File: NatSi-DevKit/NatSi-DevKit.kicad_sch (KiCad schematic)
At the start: 0 parts

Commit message: git ignore not working?
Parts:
- added U?: ESP32-S3-WROOM-1, PCM_Espressif:ESP32-S3-WROOM-1, symbol sumec_sch_lib:ESP32-S3-WROOM-1_CUSTOM_made_by_bismarx
- added U?: NCP1117-3.3_SOT223, Package_TO_SOT_SMD:SOT-223-3_TabPin2, symbol Regulator_Linear:NCP1117-3.3_SOT223
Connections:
- new net: U?.1 (GND), U?.40 (GND), U?.41 (GND)
- new net +3V3: U?.2 (3V3)

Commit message: some updates schematic
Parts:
- added C? (x3): 10uF, Capacitor_Tantalum_SMD:CP_EIA-3216-18_Kemet-A_Pad1.58x1.35mm_HandSolder, symbol Device:C_Polarized
- added C?: 100nF, Capacitor_SMD:C_0805_2012Metric_Pad1.18x1.45mm_HandSolder, symbol Device:C
- added J?: TYPE-C-31-M-12 (USB C CONN), TYPE-C-31-M-12:HRO_TYPE-C-31-M-12, symbol SchrackThingy_library:TYPE-C-31-M-12 (USB C CONN)
- gave numbers to parts that had none: 2
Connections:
- net +3V3: now also C?.1, C?.1
- net GND: now also U1.1 (GND), U1.40 (GND), U1.41 (GND), U2.1 (GND), C?.2, C?.2, C?.2, C?.2, J?.A1_B12 (GND), J?.B1_A12 (GND), J?.S1 (SHIELD), J?.S2 (SHIELD), J?.S3 (SHIELD), J?.S4 (SHIELD)
- net IO17: now reaches U1.10 (IO17)
- net IO18: now reaches U1.11 (IO18)
- net D-: now reaches U1.13 (IO19)
- net D+: now reaches U1.14 (IO20)
- net IO03: now reaches U1.15 (IO3)
- net IO42: now reaches U1.16 (IO46)
- net IO42: now also U1.35 (IO42)
- net IO21: now reaches U1.23 (IO21)
- net IO47: now reaches U1.24 (IO47)
- net IO48: now reaches U1.25 (IO48)
- net IO45: now reaches U1.26 (IO45)
- net BOOT: now reaches U1.27 (IO0)
- net IO35: now reaches U1.28 (IO35)
- net IO36: now reaches U1.29 (IO36)
- net EN: now reaches U1.3 (EN)
- net IO37: now reaches U1.30 (IO37)
- net IO38: now reaches U1.31 (IO38)
- net IO39: now reaches U1.32 (IO39)
- net IO40: now reaches U1.33 (IO40)
- net IO41: now reaches U1.34 (IO41)
- net RX: now reaches U1.36 (RXD0)
- net TX: now reaches U1.37 (TXD0)
- net IO02: now reaches U1.38 (IO2)
- net IO01: now reaches U1.39 (IO1)
- net +3.3V: now reaches U2.2 (VO)
- net +3.3V: now also C?.1
- net +5V: now reaches U2.3 (VI)
- net +5V: now also C?.1
- new net: J?.A4_B9 (VBUS), J?.B4_A9 (VBUS)
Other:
- moved on the sheet: U2

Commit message: update git ignore
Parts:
- removed J?: TYPE-C-31-M-12 (USB C CONN), TYPE-C-31-M-12:HRO_TYPE-C-31-M-12, symbol SchrackThingy_library:TYPE-C-31-M-12 (USB C CONN)
- added C?: 100nF, Capacitor_SMD:C_0805_2012Metric_Pad1.18x1.45mm_HandSolder, symbol Device:C
- added F?: Polyfuse/50R, Fuse:Fuse_0805_2012Metric, symbol Device:Polyfuse
- added J?: USB_TypeC, sumec_brd:USB_Type_C, symbol sumec_sch_lib:USB_TypeC
- added R? (x2): 15R, Resistor_SMD:R_0805_2012Metric_Pad1.20x1.40mm_HandSolder, symbol Device:R
- added U?: USBLC6-2SC6, Package_TO_SOT_SMD:TSOT-23-6_HandSoldering, symbol sumec_library:USBLC6-2SC6
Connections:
- net D+: now also U?.6
- net D-: now also U?.4
- net GND: now also C?.2, J?.A1_B12 (GND), J?.B1_A12 (GND), J?.S1 (SHIELD), J?.S2 (SHIELD), J?.S3 (SHIELD), J?.S4 (SHIELD), U?.2
- net IO04: now also U1.4 (IO4)
- net IO05: now also U1.5 (IO5)
- net IO06: now also U1.6 (IO6)
- net IO07: now also U1.7 (IO7)
- net IO08: now also U1.12 (IO8)
- net IO09: now also U1.17 (IO9)
- net IO10: now also U1.18 (IO10)
- net IO11: now also U1.19 (IO11)
- net IO12: now also U1.20 (IO12)
- net IO13: now also U1.21 (IO13)
- net IO14: now also U1.22 (IO14)
- net IO15: now also U1.8 (IO15)
- net IO16: now also U1.9 (IO16)
- new net: F?.2, J?.A4_B9 (VBUS), J?.B4_A9 (VBUS)
- new net: R?.2, U?.3
- new net: R?.2, U?.1
- new net D+ IN: J?.A6 (DP1), J?.B6 (DP2), R?.1
- new net D- IN: J?.A7 (DN1), J?.B7 (DN2), R?.1
- new net VBUS 5V: C?.1, F?.1, U?.5
- no-connect marks 0 -> 4
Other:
- note added: "ESD PROTECTION"
- note added: "GPIO USB 20 D+ (green) 19 D- (white) GND GND (black) VBUS +5V (red)"
- note added: "USB"
- note added: "USB CONNECTOR"
- note added: "USB Type-C Connector Data transfer USB connector connected to ESP32 using CDC method"

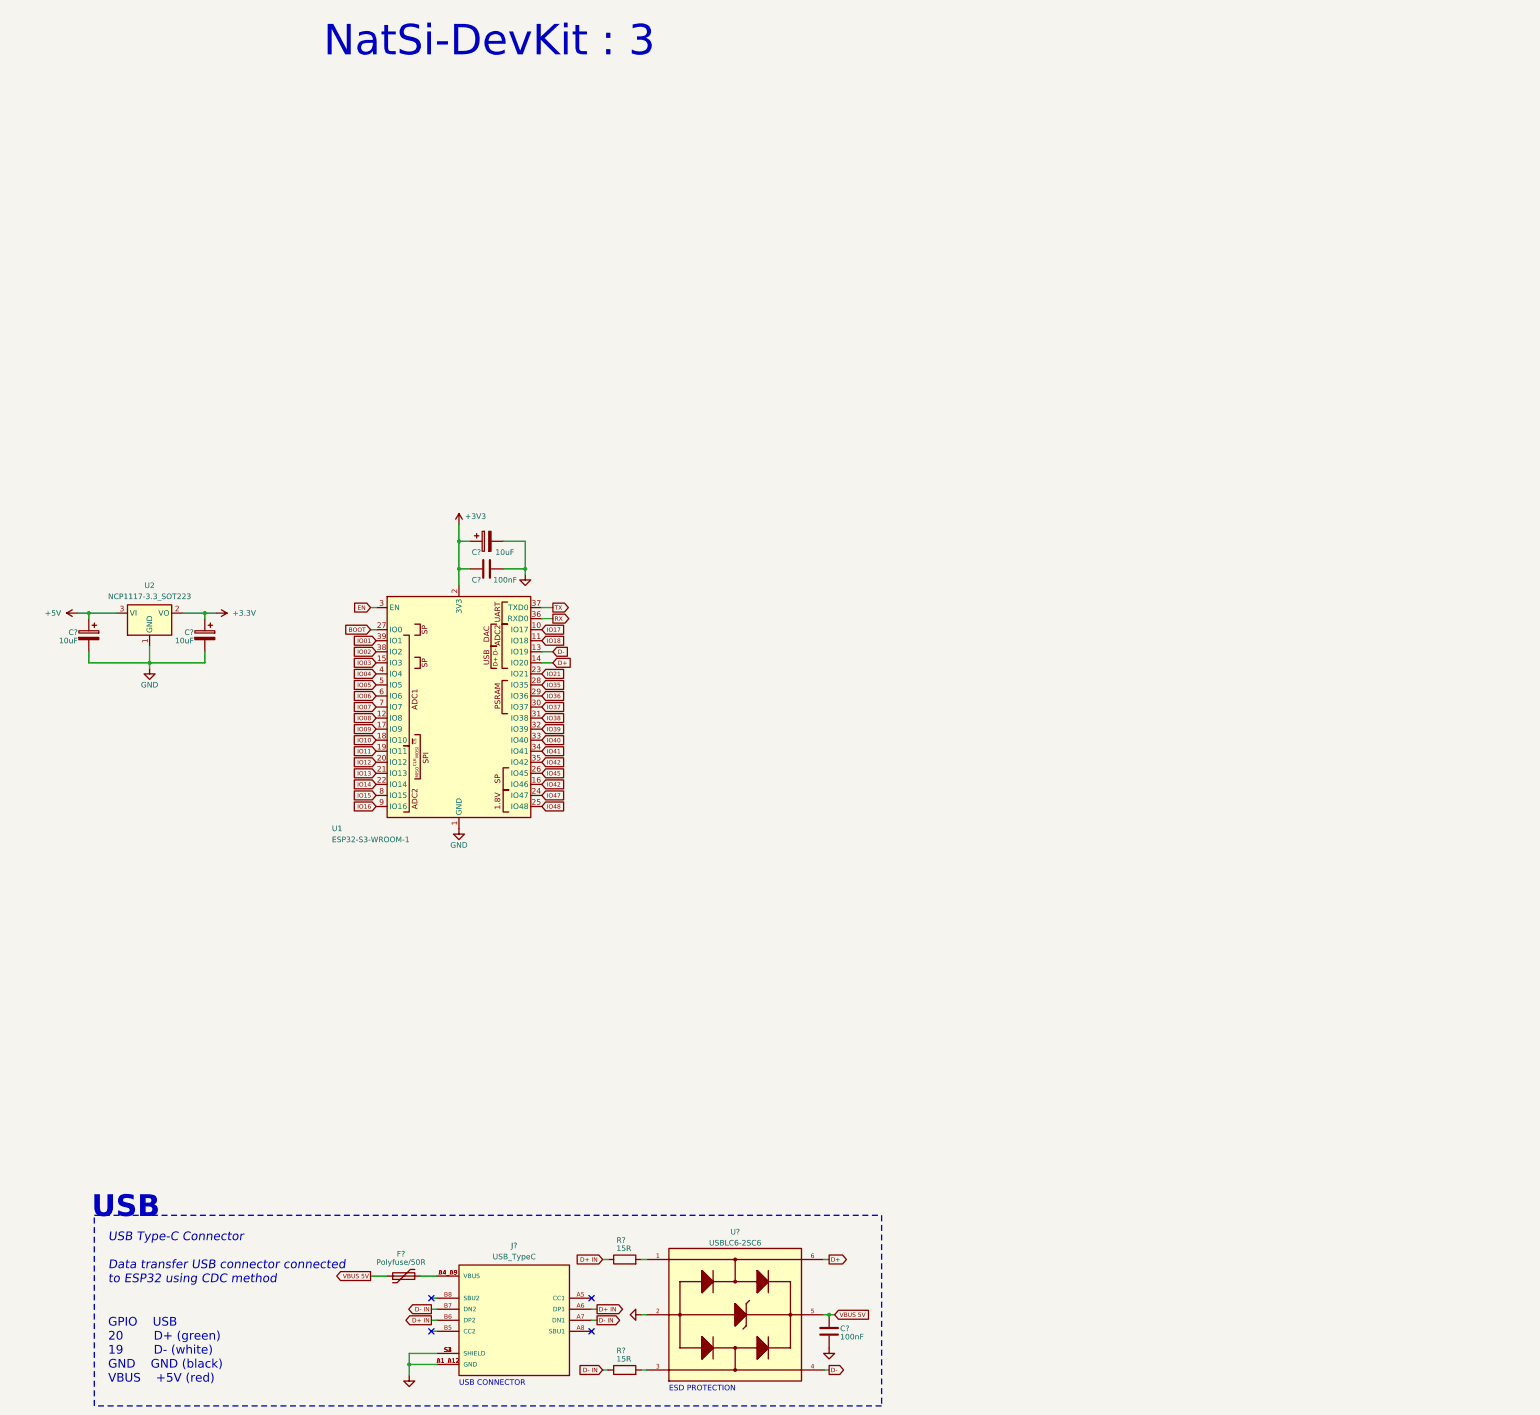
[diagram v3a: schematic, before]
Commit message: Schematic update
Blocks, schematic finished
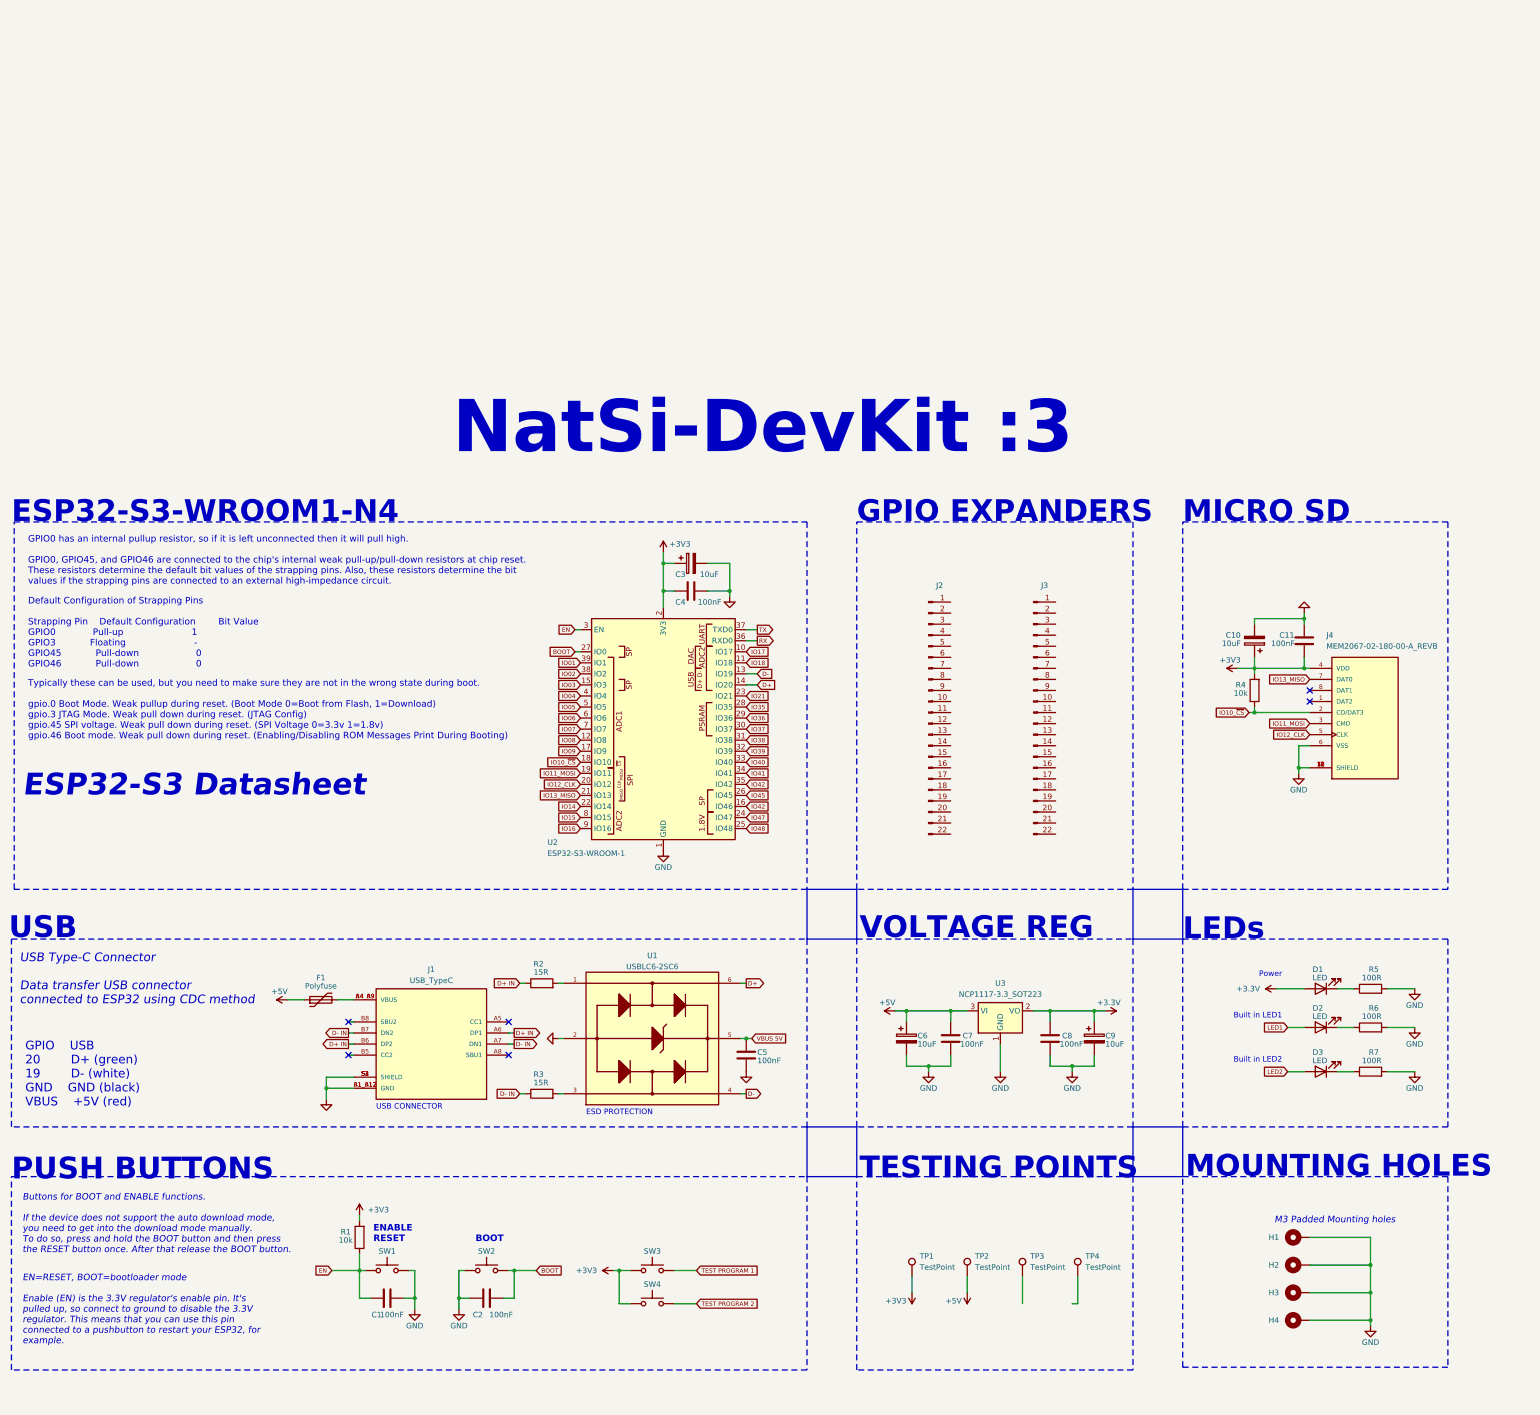
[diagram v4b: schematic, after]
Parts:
- added C1, C11, C2, C7, C8: 100nF, Capacitor_SMD:C_0805_2012Metric_Pad1.18x1.45mm_HandSolder, symbol Device:C
- added C10: 10uF, Capacitor_Tantalum_SMD:CP_EIA-3216-18_Kemet-A_Pad1.58x1.35mm_HandSolder, symbol Device:C_Polarized
- added D1, D2, D3: LED, LED_SMD:LED_0805_2012Metric_Pad1.15x1.40mm_HandSolder, symbol Device:LED
- added H1, H2, H3, H4: Mounting Hole M3, MountingHole:MountingHole_3.2mm_M3_Pad_Via, symbol Mechanical:MountingHole_Pad
- added J2, J3: Conn_01x22_Pin, Connector_PinHeader_2.54mm:PinHeader_1x22_P2.54mm_Vertical, symbol Connector:Conn_01x22_Pin
- added J4: MEM2067-02-180-00-A_REVB, Schrack_brd:MICRO_SD_CARD, symbol SchrackThingy_library:MEM2067-02-180-00-A_REVB
- added R1, R4: 10k, Resistor_SMD:R_0805_2012Metric_Pad1.20x1.40mm_HandSolder, symbol Device:R
- added R5, R6, R7: 100R, Resistor_SMD:R_0805_2012Metric_Pad1.20x1.40mm_HandSolder, symbol Device:R
- added SW1, SW2, SW3, SW4: SW_Push, Button_Switch_SMD:SW_SPST_EVQPE1, symbol Switch:SW_Push
- added TP1, TP2, TP3, TP4: TestPoint, TestPoint:TestPoint_Pad_1.0x1.0mm, symbol Connector:TestPoint
- F1: renamed from F?; value Polyfuse/50R -> Polyfuse
- gave numbers to parts that had none: 9
- renumbered U1 to U2, U2 to U3
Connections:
- net +3.3V: now also C8.2, D1.2 (A)
- net +3V3: now also C10.1, C11.1, J4.4 (VDD), R1.2, R4.2, SW3.1, SW4.1, TP1.1
- net +5V: now also F1.1, C7.2, TP2.1
- net BOOT: now also C2.1, SW2.2
- net EN: now also C1.1, R1.1, SW1.2
- net GND: now also C1.2, C10.2, C11.2, C2.2, C7.1, C8.1, H1.1, H2.1, H3.1, H4.1, J4.10 (SHIELD), J4.11 (SHIELD), J4.12 (SHIELD), J4.6 (VSS), J4.9 (SHIELD), R5.2, R6.2, R7.2, SW1.1, SW2.1
- net VBUS 5V: no longer F1.1
- net IO10 renamed IO10_~{CS}
- net IO10_~{CS}: now also J4.2 (CD/DAT3), R4.1
- net IO11 renamed IO11_MOSI
- net IO11_MOSI: now also J4.3 (CMD)
- net IO12 renamed IO12_CLK
- net IO12_CLK: now also J4.5 (CLK)
- net IO13 renamed IO13_MISO
- net IO13_MISO: now also J4.7 (DAT0)
- new net: D3.1 (K), R7.1
- new net: D2.1 (K), R6.1
- new net: D1.1 (K), R5.1
- new net LED1: D2.2 (A)
- new net LED2: D3.2 (A)
- new net TEST PROGRAM 1: SW3.2
- new net TEST PROGRAM 2: SW4.2
- no-connect marks 4 -> 6
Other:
- note added: "BOOT"
- note added: "Built in LED1"
- note added: "Built in LED2"
- note added: "Buttons for BOOT and ENABLE functions. If the device does not support the auto download mode, you need to get into the download mode manually. To do so, press and hold the BOOT button and then press the RESET button once. After that release the BOOT button."
- note added: "Default Configuration of Strapping Pins Strapping Pin Default Configuration Bit Value GPIO0 Pull-up 1 GPIO3 Floating - GPIO45 Pull-down 0 GPIO46 Pull-down 0"
- note added: "EN=RESET, BOOT=bootloader mode Enable (EN) is the 3.3V regulator's enable pin. It's pulled up, so connect to ground to disable the 3.3V regulator. This means that you can use this pin connected to a pushbutton to restart your ESP32, for example."
- note added: "ENABLE RESET"
- note added: "ESP32-S3 Datasheet"
- note added: "ESP32-S3-WROOM1-N4"
- note added: "GPIO EXPANDERS"
- note added: "GPIO0 has an internal pullup resistor, so if it is left unconnected then it will pull high. GPIO0, GPIO45, and GPIO46 are connected to the chip's internal weak pull-up/pull-down resistors at chip reset. These resistors determine the default bit values of the strapping pins. Also, these resistors determine the bit values if the strapping pins are connected to an external high-impedance circuit."
- note added: "LEDs"
- note added: "M3 Padded Mounting holes"
- note added: "MICRO SD"
- note added: "MOUNTING HOLES"
- note added: "NatSi-DevKit :3"
- note added: "PUSH BUTTONS"
- note added: "Power"
- note added: "TESTING POINTS"
- note added: "Typically these can be used, but you need to make sure they are not in the wrong state during boot. gpio.0 Boot Mode. Weak pullup during reset. (Boot Mode 0=Boot from Flash, 1=Download) gpio.3 JTAG Mode. Weak pull down during reset. (JTAG Config) gpio.45 SPI voltage. Weak pull down during reset. (SPI Voltage 0=3.3v 1=1.8v) gpio.46 Boot mode. Weak pull down during reset. (Enabling/Disabling ROM Me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"
- note added: "VOLTAGE REG"
- note removed: "NatSi-DevKit : 3"
- moved on the sheet: C3, C4, C5, C6, C9, F1, J1, R2, R3, U1, U2, U3

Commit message: layout update
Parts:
- removed SW4: SW_Push, Button_Switch_SMD:SW_SPST_EVQPE1, symbol Switch:SW_Push
- added C1, C13: 100nF, Capacitor_SMD:C_0805_2012Metric_Pad1.18x1.45mm_HandSolder, symbol Device:C
- added D1: D_Schottky, Diode_SMD:D_1206_3216Metric_Pad1.42x1.75mm_HandSolder, symbol Device:D_Schottky
- added R1: 100k, Resistor_SMD:R_0805_2012Metric_Pad1.20x1.40mm_HandSolder, symbol Device:R
- added R?: 1k, Resistor_SMD:R_0805_2012Metric_Pad1.20x1.40mm_HandSolder, symbol Device:R
- added R?: 10k, Resistor_SMD:R_0805_2012Metric_Pad1.20x1.40mm_HandSolder, symbol Device:R
- H1, H2, H3, H4: footprint MountingHole:MountingHole_3.2mm_M3_Pad_Via -> MountingHole:MountingHole_2.1mm
- renumbered C9 to C10, C10 to C11, C11 to C12, C1 to C2, C2 to C3, C3 to C4, C4 to C5, C5 to C6, C6 to C7, C7 to C8, C8 to C9, D1 to D2, D2 to D3, D3 to D4, R1 to R2, R2 to R3, R3 to R4, R4 to R5, R5 to R6, R6 to R7, R7 to R8
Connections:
- net +3.3V is gone; now on net +3V3: C10.1, C9.2, D2.2 (A), U3.2 (VO)
- net VBUS 5V is gone; now on net +5V: C6.1, U1.5
- net +3V3: now also R?.2; no longer SW3.1
- net +5V: now also D1.1 (K); no longer F1.1
- net GND: now also SW3.1, C1.1, C13.1, R1.2; no longer J1.S1 (SHIELD), J1.S2 (SHIELD), J1.S3 (SHIELD), J1.S4 (SHIELD)
- net TEST PROGRAM 1: no longer names the net of SW3.2
- net TEST PROGRAM 1: now also R?.1
- new net: D1.2 (A), F1.1
- new net BT1: C13.2, R?.1, R?.2
- new net SHLD: C1.2, J1.S1 (SHIELD), J1.S2 (SHIELD), J1.S3 (SHIELD), J1.S4 (SHIELD), R1.1
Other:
- moved on the sheet: C6, J1, R3, R4, U1

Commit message: pcb layout
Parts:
- removed H1, H2, H3, H4: Mounting Hole M3, MountingHole:MountingHole_2.1mm, symbol Mechanical:MountingHole_Pad
- removed R6, R7: 100R, Resistor_SMD:R_0805_2012Metric_Pad1.20x1.40mm_HandSolder, symbol Device:R
- added R10, R9: 100R, Resistor_SMD:R_0805_2012Metric_Pad1.20x1.40mm_HandSolder, symbol Device:R
- TP1, TP2, TP3: footprint TestPoint:TestPoint_Pad_1.0x1.0mm -> TestPoint:TestPoint_THTPad_D1.5mm_Drill0.7mm
- TP4: footprint TestPoint:TestPoint_Pad_1.0x1.0mm -> sumec_graphic:NATI_PICME_IMG
- gave numbers to parts that had none: 2
- renumbered C9 to C10, C10 to C11, C11 to C12, C12 to C13, C13 to C6, C6 to C7, C7 to C8, C8 to C9, R5 to R7
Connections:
- net +3V3: now also R8.1; no longer D2.2 (A)
- net GND: now also D2.1 (K), D3.1 (K), D4.1 (K), TP3.1; no longer R8.2
- net LED1: now also R9.1; no longer D3.2 (A)
- net LED2: now also R10.1; no longer D4.2 (A)
- new net: D2.2 (A), R8.2
- new net: D4.2 (A), R10.2
- new net: D3.2 (A), R9.2
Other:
- moved on the sheet: C6, R6
